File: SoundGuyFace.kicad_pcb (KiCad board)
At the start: 2 copper layers, 55.1 x 46.5 mm, 74 parts, among them J1 NRJ6HF-1, J2 NCJ6FA-H-0, J3 UJ2-MIBH-4-MSMT-TR, U1 PCM2912A, U2 INA333, U3 TPS61041DBV, Y1 6MHz

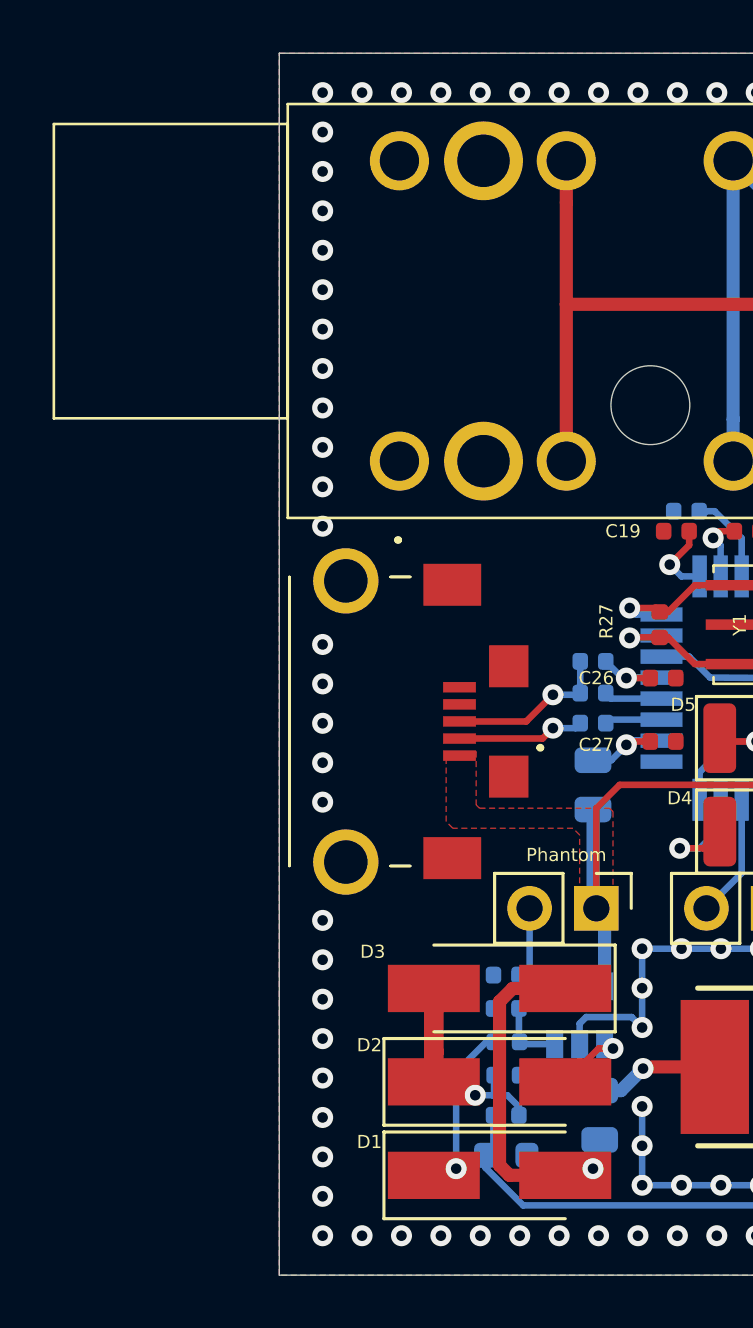
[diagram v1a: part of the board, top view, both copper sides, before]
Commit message: First Hardware debug. Forgot sparing for the USB connector
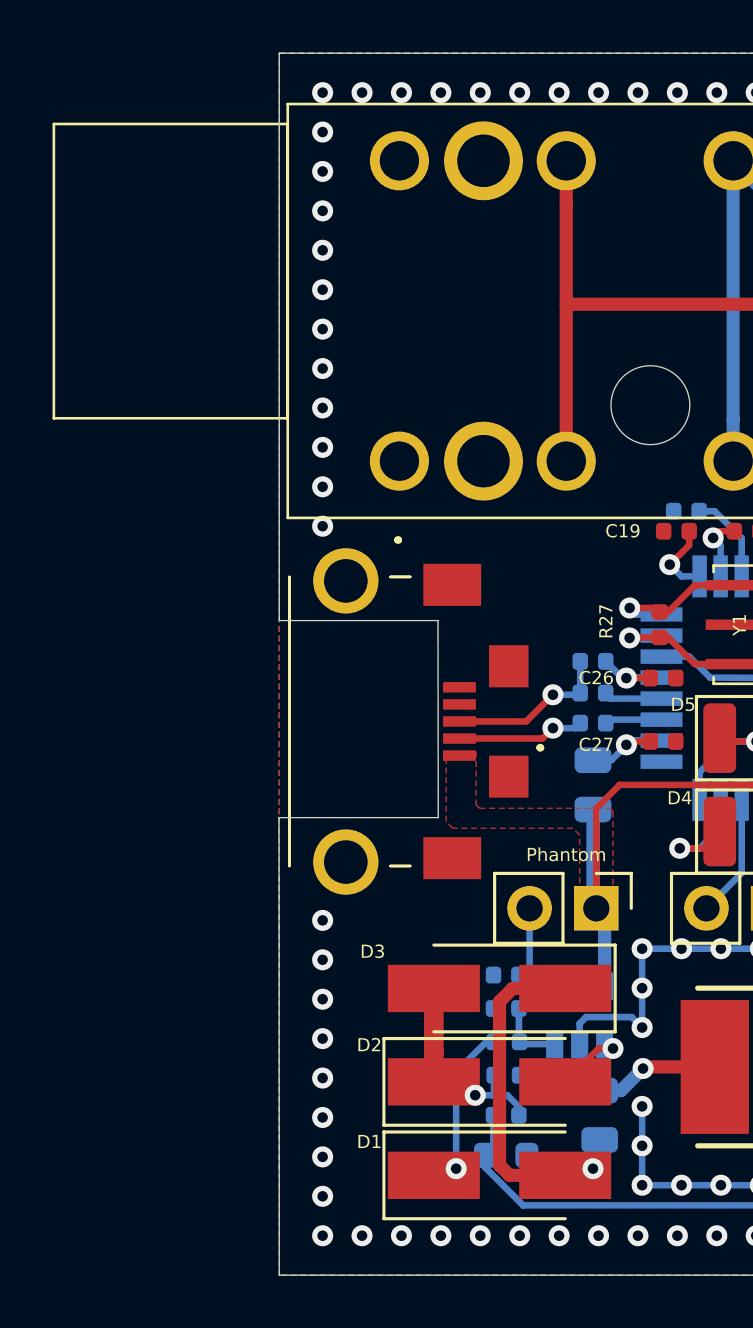
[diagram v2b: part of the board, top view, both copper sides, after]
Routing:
- net GND: vias 160 -> 155
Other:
- outline, holes or cut-outs redrawn
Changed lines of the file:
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@@
   (general
     (thickness 1.6)
-    (drawings 11)
-    (tracks 605)
+    (drawings 15)
+    (tracks 600)
     (zones 0)
     (modules 74)
@@
   )
   (layers
-    (0 F.Cu signal hide)
+    (0 F.Cu signal)
     (31 B.Cu signal hide)
     (32 B.Adhes user hide)
@@
     (34 B.Paste user hide)
     (35 F.Paste user hide)
-    (36 B.SilkS user)
-    (37 F.SilkS user)
+    (36 B.SilkS user hide)
+    (37 F.SilkS user hide)
     (38 B.Mask user hide)
     (39 F.Mask user hide)
     (40 Dwgs.User user hide)
-    (41 Cmts.User user)
+    (41 Cmts.User user hide)
     (42 Eco1.User user hide)
     (43 Eco2.User user hide)
@@
     )
   )
+  (gr_line (start 133.35 71.09) (end 133.35 49.5) (layer Edge.Cuts) (width 0.05))
+  (gr_line (start 139.39 71.09) (end 133.35 71.09) (layer Edge.Cuts) (width 0.05))
+  (gr_line (start 139.4 78.59) (end 139.39 71.09) (layer Edge.Cuts) (width 0.05))
+  (gr_line (start 133.34 78.59) (end 139.4 78.59) (layer Edge.Cuts) (width 0.05))
+  (gr_line (start 133.35 96) (end 133.34 78.59) (layer Edge.Cuts) (width 0.05))
   (gr_text F (at 178.689 89.662) (layer B.SilkS)
     (effects (font (size 4 4) (thickness 1)) (justify mirror))
@@
     (arrow2b (pts (xy 133.35 98.298) (xy 134.476504 97.711579)))
   )
-  (gr_line (start 133.35 96) (end 133.35 49.5) (layer Edge.Cuts) (width 0.05))
   (gr_line (start 188.468 96) (end 133.35 96) (layer Edge.Cuts) (width 0.05))
   (gr_line (start 188.468 49.5) (end 188.468 96) (layer Edge.Cuts) (width 0.05))
@@
   (via (at 135 87) (size 0.8) (drill 0.4) (layers F.Cu B.Cu) (net 4))
   (via (at 135 84) (size 0.8) (drill 0.4) (layers F.Cu B.Cu) (net 4))
-  (via (at 135 78) (size 0.8) (drill 0.4) (layers F.Cu B.Cu) (net 4))
   (via (at 135 85.5) (size 0.8) (drill 0.4) (layers F.Cu B.Cu) (net 4))
   (via (at 135 82.5) (size 0.8) (drill 0.4) (layers F.Cu B.Cu) (net 4))
-  (via (at 135 72) (size 0.8) (drill 0.4) (layers F.Cu B.Cu) (net 4))
-  (via (at 135 73.5) (size 0.8) (drill 0.4) (layers F.Cu B.Cu) (net 4))
-  (via (at 135 75) (size 0.8) (drill 0.4) (layers F.Cu B.Cu) (net 4))
-  (via (at 135 76.5) (size 0.8) (drill 0.4) (layers F.Cu B.Cu) (net 4))
   (via (at 135 60) (size 0.8) (drill 0.4) (layers F.Cu B.Cu) (net 4))
   (via (at 135 66) (size 0.8) (drill 0.4) (layers F.Cu B.Cu) (net 4))
@@
       )
     )
+  )
+  (zone (net 0) (net_name "") (layers F&B.Cu) (hatch edge 0.508)
+    (connect_pads (clearance 0.254))
+    (min_thickness 0.254)
+    (keepout (tracks not_allowed) (vias not_allowed) (copperpour not_allowed))
+    (fill (arc_segments 32) (thermal_gap 0.508) (thermal_bridge_width 0.508))
+    (polygon
+      (pts
+        (xy 139.39 71.1) (xy 139.39 78.59) (xy 133.34 78.6) (xy 133.35 71.08)
+      )
+    )
